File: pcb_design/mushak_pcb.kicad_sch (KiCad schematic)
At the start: 48 parts, among them J1 Conn_01x04_Male, J10 IR_1, J11 AS5600_1, J12 IR_2, J13 AS5600_2, J14 IR_3, J15 ToF, J16 IR_4, J2 Conn_01x02_Female, J3 BLE_Conn, Q1 DMN3065LW-7, SW1 SW_Push, SW2 SW_Push, U1 BA30BC0FP-E2, U6 STM32F405RGTx, Y1 25Mhz, Y2 32.769kHz

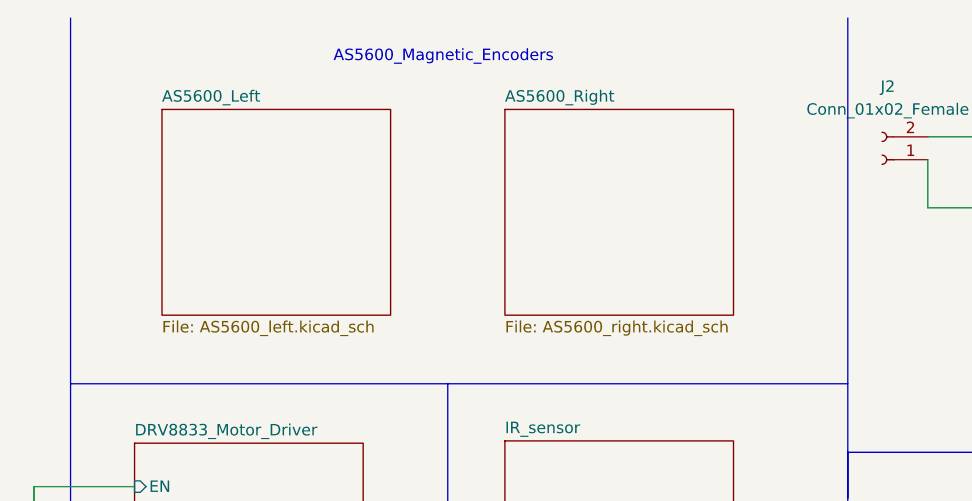
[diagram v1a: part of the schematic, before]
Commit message: modified capacitors for encoders
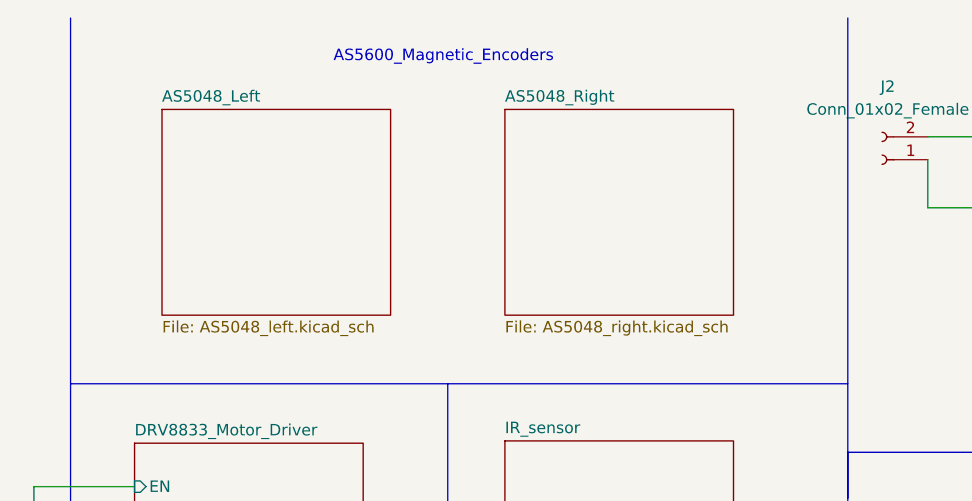
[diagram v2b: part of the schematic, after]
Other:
- sheet AS5600_Left renamed AS5048_Left
- sheet AS5600_Right renamed AS5048_Right
- sheet AS5048_Left: file AS5600_left.kicad_sch -> AS5048_left.kicad_sch
- sheet AS5048_Right: file AS5600_right.kicad_sch -> AS5048_right.kicad_sch
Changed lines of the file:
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@@
     (stroke (width 0.1524) (type solid) (color 0 0 0 0))
     (fill (color 0 0 0 0.0000))
-    (property "Sheet name" "AS5600_Right" (id 0) (at 143.51 22.1484 0)
-      (effects (font (size 1.27 1.27)) (justify left bottom))
-    )
-    (property "Sheet file" "AS5600_right.kicad_sch" (id 1) (at 143.51 46.3046 0)
+    (property "Sheet name" "AS5048_Right" (id 0) (at 143.51 22.1484 0)
+      (effects (font (size 1.27 1.27)) (justify left bottom))
+    )
+    (property "Sheet file" "AS5048_right.kicad_sch" (id 1) (at 143.51 46.3046 0)
       (effects (font (size 1.27 1.27)) (justify left top))
     )
@@
     (stroke (width 0.1524) (type solid) (color 0 0 0 0))
     (fill (color 0 0 0 0.0000))
-    (property "Sheet name" "AS5600_Left" (id 0) (at 105.41 22.1484 0)
-      (effects (font (size 1.27 1.27)) (justify left bottom))
-    )
-    (property "Sheet file" "AS5600_left.kicad_sch" (id 1) (at 105.41 46.3046 0)
+    (property "Sheet name" "AS5048_Left" (id 0) (at 105.41 22.1484 0)
+      (effects (font (size 1.27 1.27)) (justify left bottom))
+    )
+    (property "Sheet file" "AS5048_left.kicad_sch" (id 1) (at 105.41 46.3046 0)
       (effects (font (size 1.27 1.27)) (justify left top))
     )
@@
     )
     (path "/21ce20a6-b7bb-4e01-a357-9d2d3872aa77/3c0c9c03-9063-4d7b-9973-5baea752bcbf"
-      (reference "C22") (unit 1) (value "0.1uF") (footprint "Capacitor_SMD:C_0402_1005Metric")
+      (reference "C22") (unit 1) (value "10uF") (footprint "Capacitor_SMD:C_0603_1608Metric")
     )
     (path "/b79b66d4-5cc5-4098-8c09-408f16b669f0/5c07921a-d9ee-4218-b14f-44f9225af66e"
-      (reference "C23") (unit 1) (value "0.1uF") (footprint "Capacitor_SMD:C_0402_1005Metric")
+      (reference "C23") (unit 1) (value "10uF") (footprint "Capacitor_SMD:C_0603_1608Metric")
     )
     (path "/33d216d7-8249-4d7f-8be9-47abab609a3e"

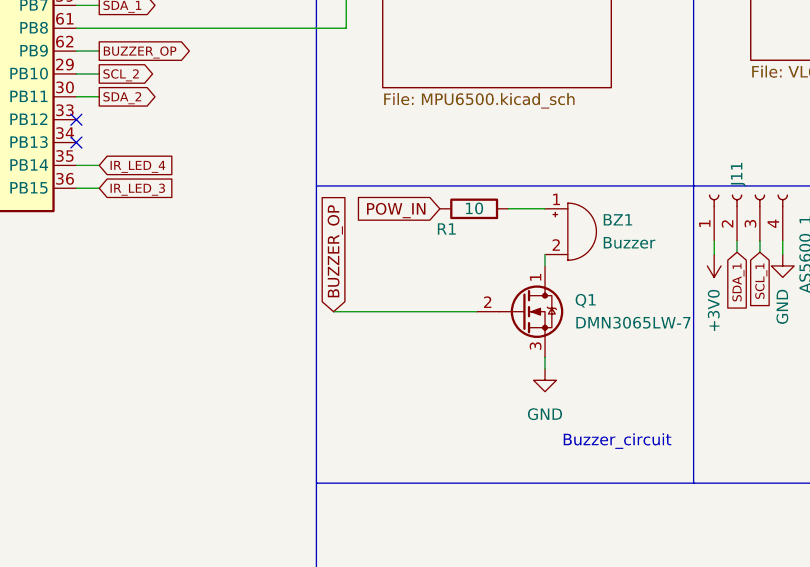
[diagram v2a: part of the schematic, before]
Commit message: Add resistors between MOSFET gate
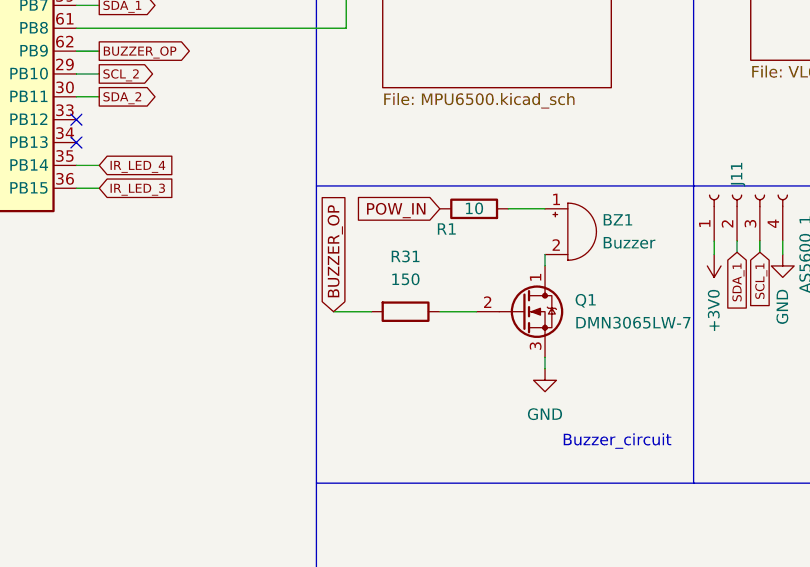
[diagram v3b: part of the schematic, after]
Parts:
- added R31: 150, Resistor_SMD:R_0402_1005Metric, symbol Device:R
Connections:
- net BUZZER_OP: now also R31.2; no longer Q1.2 (G)
- new net: Q1.2 (G), R31.1
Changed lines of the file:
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@@
+    (stroke (width 0) (type default) (color 0 0 0 0))
+  )
+  (wire (pts (xy 108.966 147.32) (xy 113.03 147.32))
     (stroke (width 0) (type default) (color 0 0 0 0))
   )
@@
     (stroke (width 0) (type default) (color 0 0 0 0))
   )
-  (wire (pts (xy 97.155 147.32) (xy 113.03 147.32))
+  (wire (pts (xy 97.155 147.32) (xy 101.346 147.32))
     (stroke (width 0) (type default) (color 0 0 0 0))
   )
@@
     (pin "9")
   )
+  (symbol (lib_id "Device:R") (at 105.156 147.32 270) (unit 1)
+    (in_bom yes) (on_board yes) (fields_autoplaced)
+    (property "Reference" "R31" (id 0) (at 105.156 141.224 90))
+    (property "Value" "150" (id 1) (at 105.156 143.764 90))
+    (property "Footprint" "Resistor_SMD:R_0402_1005Metric" (id 2) (at 105.156 145.542 90)
+      (effects (font (size 1.27 1.27)) hide)
+    )
+    (property "Datasheet" "~" (id 3) (at 105.156 147.32 0)
+      (effects (font (size 1.27 1.27)) hide)
+    )
+    (pin "1")
+    (pin "2")
+  )
   (symbol (lib_id "Device:C") (at 270.51 93.98 0) (unit 1)
     (in_bom yes) (on_board yes) (fields_autoplaced)
@@
       (reference "R26") (unit 1) (value "10k") (footprint "Resistor_SMD:R_0402_1005Metric")
     )
+    (path "/d3d22231-fa9b-4591-9863-4fcf67893a0c/247a1da8-04cf-4a61-9d87-cedbd5bdee00"
+      (reference "R27") (unit 1) (value "150") (footprint "Resistor_SMD:R_0402_1005Metric")
+    )
+    (path "/d3d22231-fa9b-4591-9863-4fcf67893a0c/bf131b8a-7170-4c33-8ede-edaf3279adb8"
+      (reference "R28") (unit 1) (value "150") (footprint "Resistor_SMD:R_0402_1005Metric")
+    )
+    (path "/d3d22231-fa9b-4591-9863-4fcf67893a0c/a5786716-06ae-48c1-b6d5-92f8121dcc19"
+      (reference "R29") (unit 1) (value "150") (footprint "Resistor_SMD:R_0402_1005Metric")
+    )
+    (path "/d3d22231-fa9b-4591-9863-4fcf67893a0c/18af4732-76c9-479b-83fc-1018c327dd6b"
+      (reference "R30") (unit 1) (value "150") (footprint "Resistor_SMD:R_0402_1005Metric")
+    )
+    (path "/96eb8848-8d99-4323-a927-23b24186bfdc"
+      (reference "R31") (unit 1) (value "150") (footprint "Resistor_SMD:R_0402_1005Metric")
+    )
     (path "/b266ad3c-1d50-4b2b-8a1e-c69f93195963"

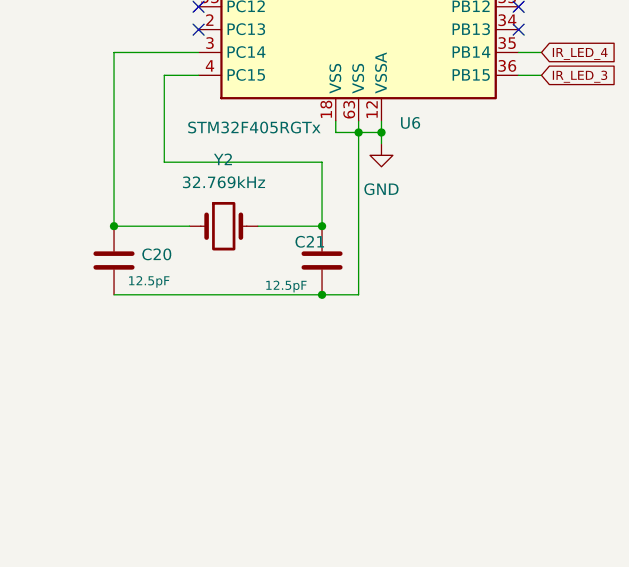
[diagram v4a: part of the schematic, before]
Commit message: Update PCB as per manufacturing requirements
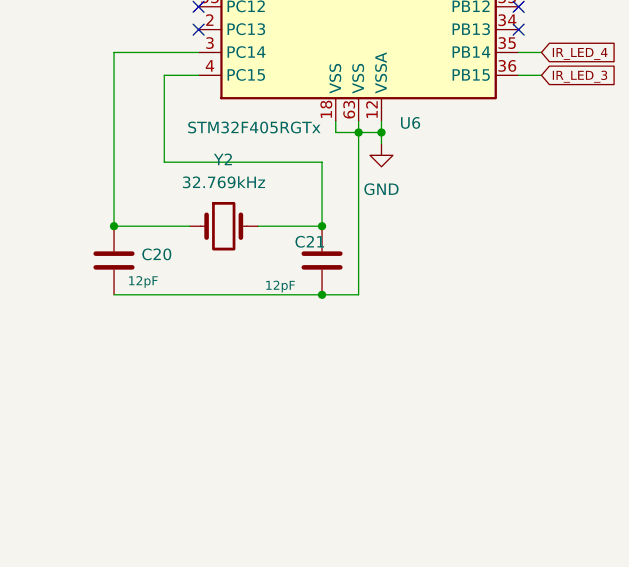
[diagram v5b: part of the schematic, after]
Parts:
- C20, C21: value 12.5pF -> 12pF
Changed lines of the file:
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@@
       (effects (font (size 1.27 1.27)) (justify left))
     )
-    (property "Value" "12.5pF" (id 1) (at 25.146 156.464 0)
+    (property "Value" "12pF" (id 1) (at 25.146 156.464 0)
       (effects (font (size 1 1)) (justify left))
     )
@@
       (effects (font (size 1.27 1.27)) (justify left))
     )
-    (property "Value" "12.5pF" (id 1) (at 40.386 156.972 0)
+    (property "Value" "12pF" (id 1) (at 40.386 156.972 0)
       (effects (font (size 1 1)) (justify left))
     )
@@
     )
     (path "/24daa530-52f3-4b5d-b3e4-9566134f88a7"
-      (reference "C20") (unit 1) (value "12.5pF") (footprint "Capacitor_SMD:C_0402_1005Metric")
+      (reference "C20") (unit 1) (value "12pF") (footprint "Capacitor_SMD:C_0402_1005Metric")
     )
     (path "/52577cb3-f0fb-427a-8f19-6df3d1f7745e"
-      (reference "C21") (unit 1) (value "12.5pF") (footprint "Capacitor_SMD:C_0402_1005Metric")
+      (reference "C21") (unit 1) (value "12pF") (footprint "Capacitor_SMD:C_0402_1005Metric")
     )
     (path "/21ce20a6-b7bb-4e01-a357-9d2d3872aa77/3c0c9c03-9063-4d7b-9973-5baea752bcbf"

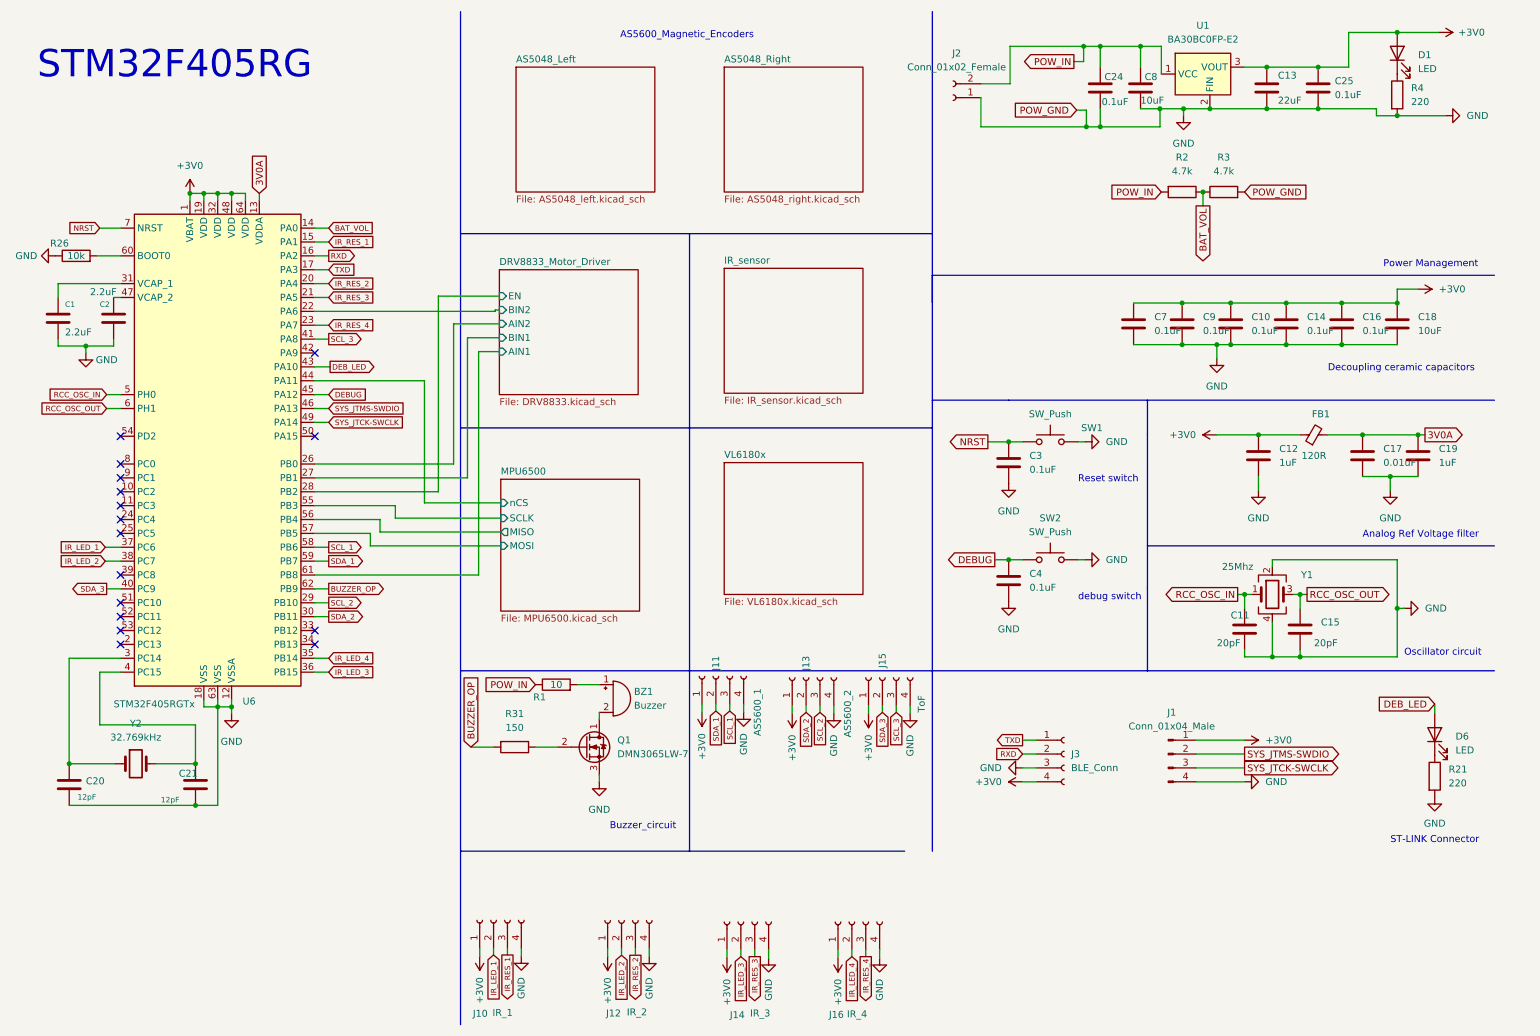
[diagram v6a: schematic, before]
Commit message: Update Mushak PCB design to include new features (#5)
* Update mushak PCB with new changes
* Add AMS1117 as 3.3v regulator
* Add new alternate placement for IR sensors
* Add new 3.3v compatible ToF sensor
* Update gerber files

* Add changes to silkscreen and filter capacitors
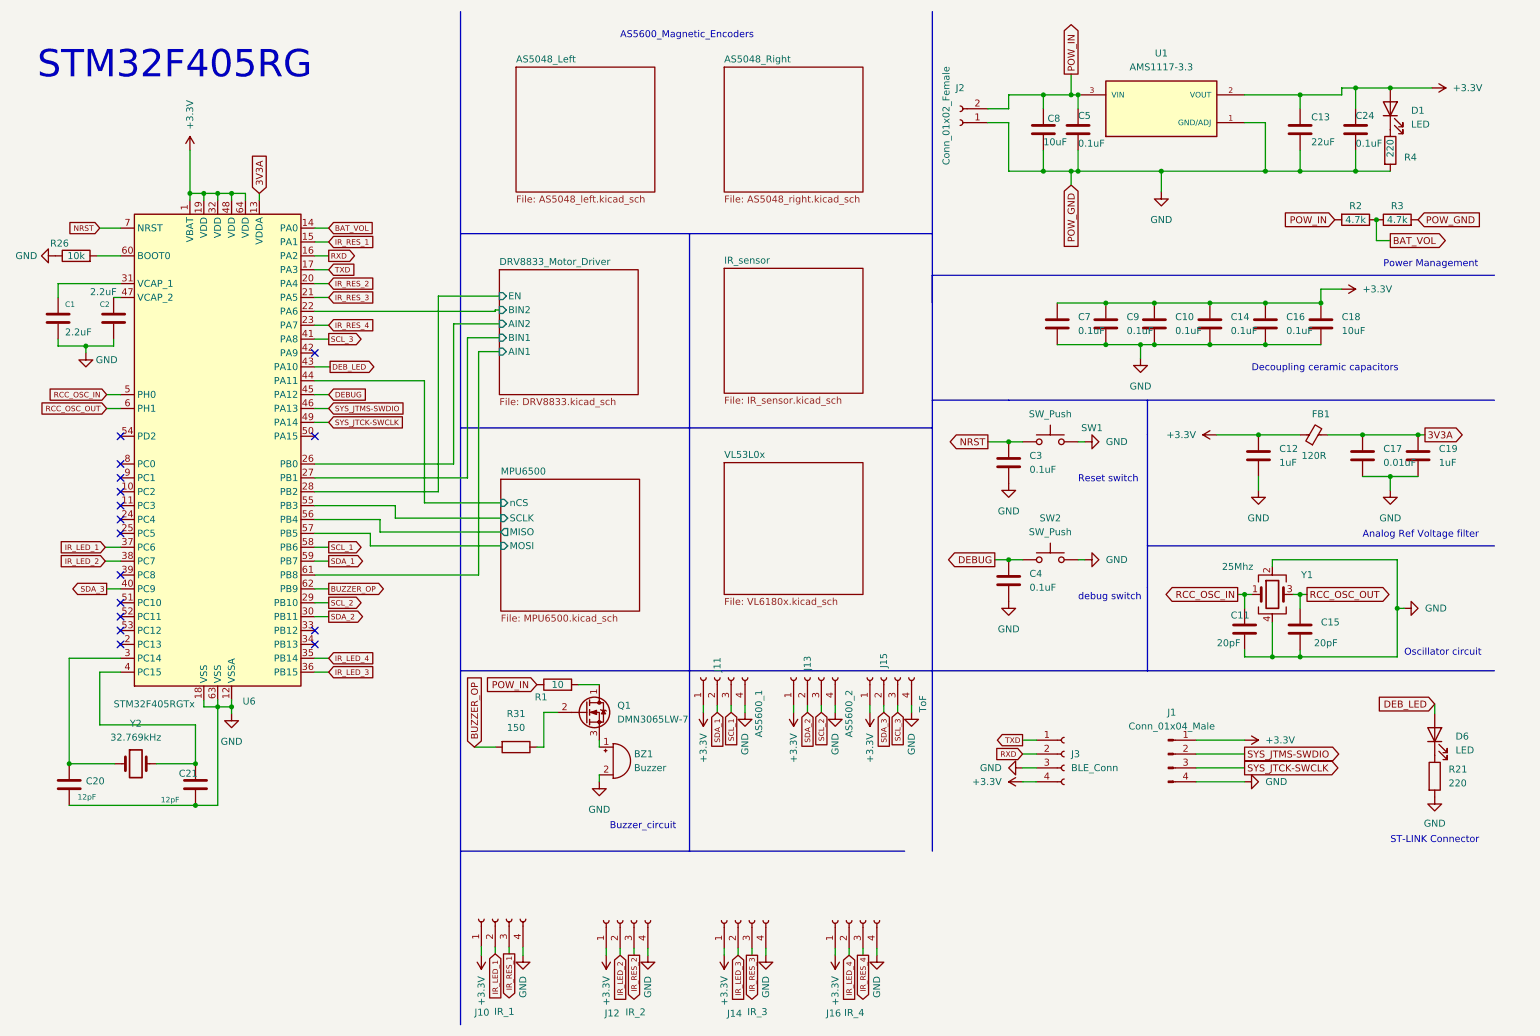
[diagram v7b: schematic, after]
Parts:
- removed C25: 0.1uF, Capacitor_SMD:C_0402_1005Metric, symbol Device:C
- removed U1: BA30BC0FP-E2, IPD50P04P4L-11:DPAK228P998X235-3N, symbol BA30BC0FP-E2:BA30BC0FP-E2
- added C5: 0.1uF, Capacitor_SMD:C_0402_1005Metric, symbol Device:C
- added U1: AMS1117-3.3, AMS1117-3:SOT229P700X180-4N, symbol AMS1117-3.3:AMS1117-3.3
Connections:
- net GND: now also BZ1.2 (+), C5.2, U1.1 (GND/ADJ); no longer Q1.3 (S)
- net POW_IN: now also C5.1, U1.3 (VIN); no longer C24.1
- net at R1.2: now also Q1.1 (D); no longer BZ1.1 (-)
- net +3V0 renamed +3.3V
- net +3.3V: now also C24.1, U1.2 (VOUT)
- net 3V0A renamed 3V3A
- new net: BZ1.1 (-), Q1.3 (S)
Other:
- sheet VL6180x renamed VL53L0x
- moved on the sheet: BZ1, C10, C13, C14, C16, C18, C7, C8, C9, D1, J14, J16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
